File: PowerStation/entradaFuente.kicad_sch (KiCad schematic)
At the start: 0 parts

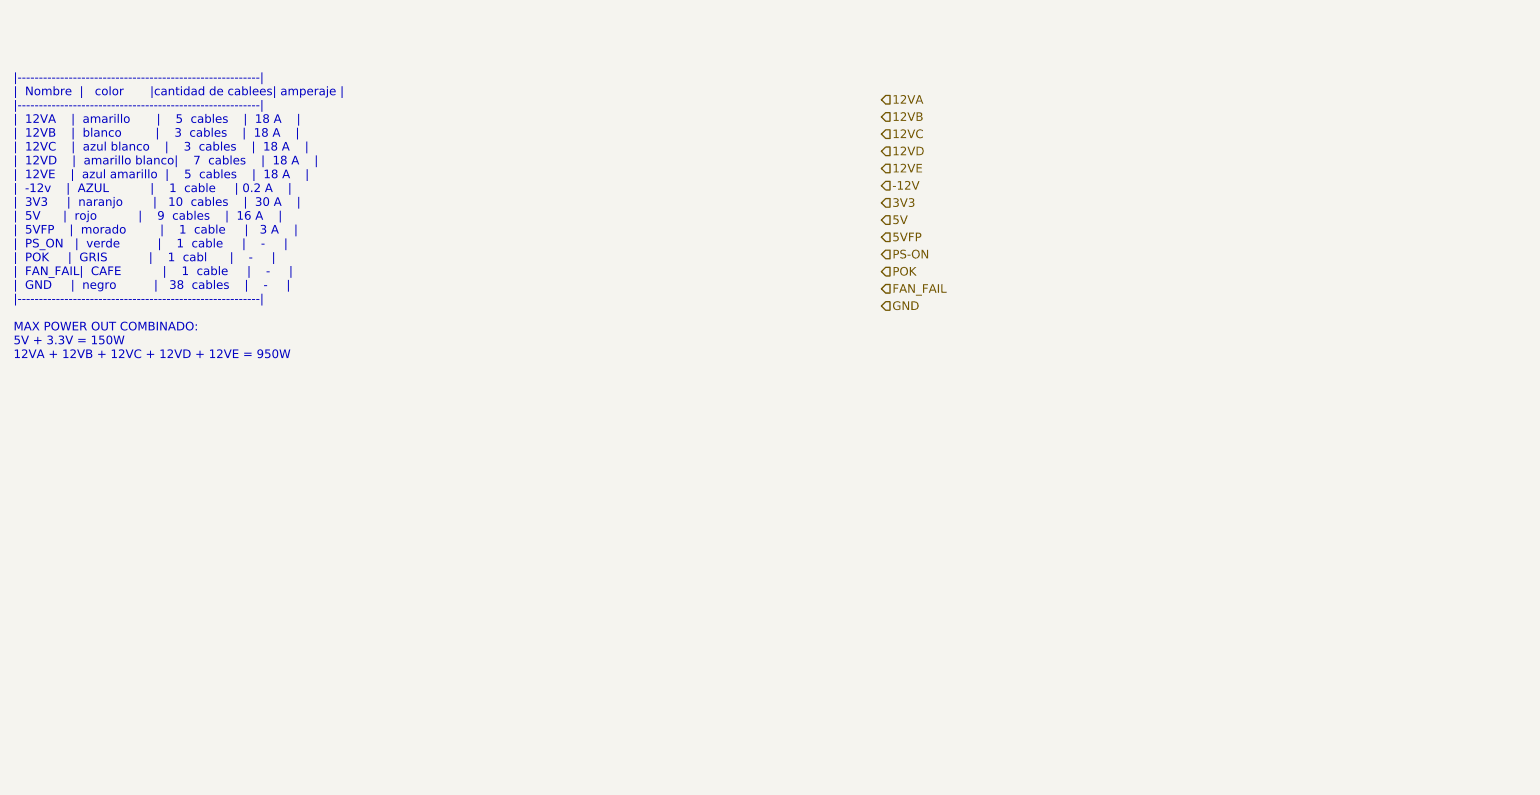
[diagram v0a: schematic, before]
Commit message: terminando diagrama
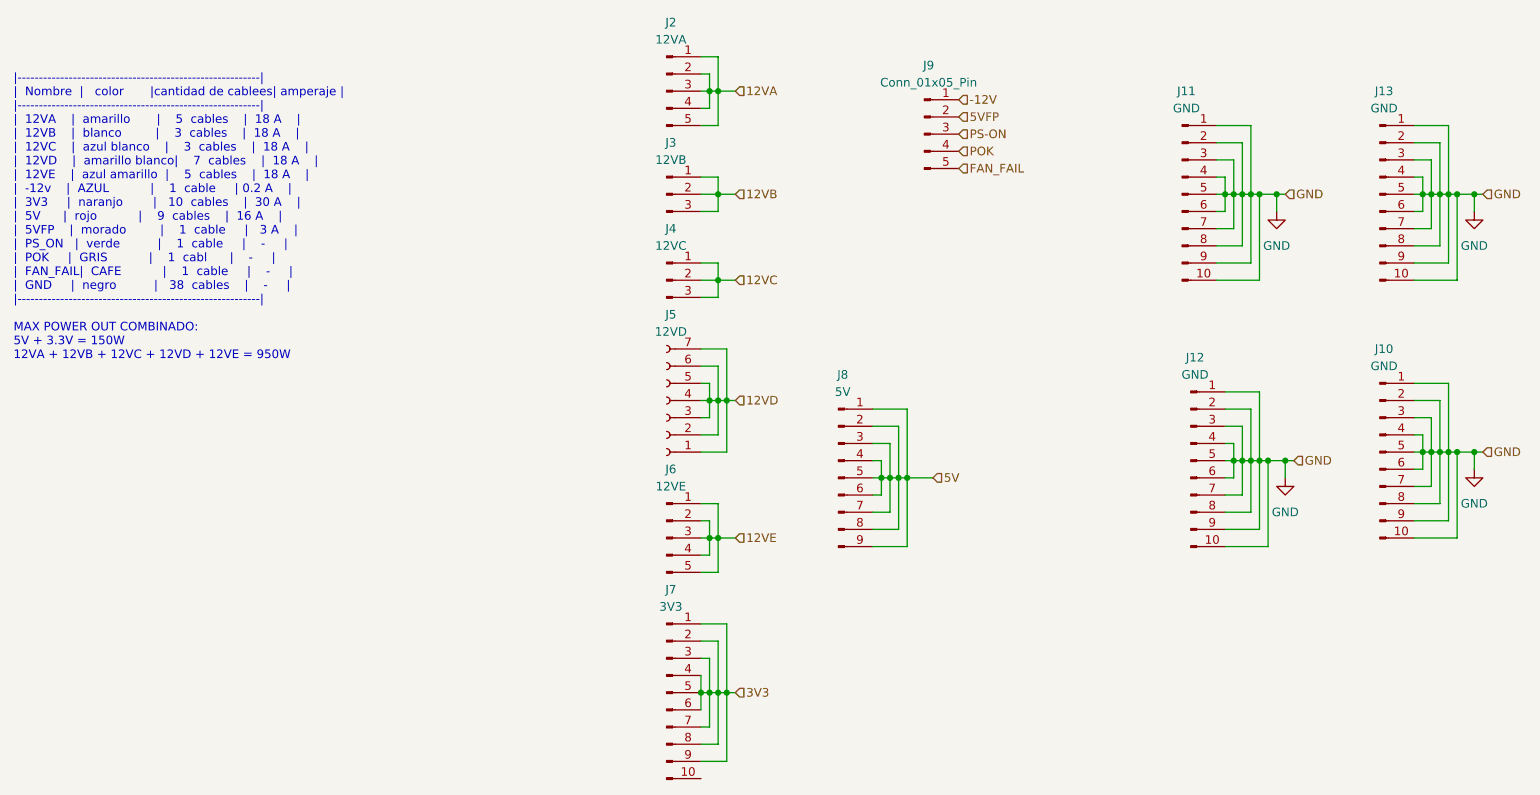
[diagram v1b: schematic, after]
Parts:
- added J10, J11, J12, J13: GND, symbol Connector:Conn_01x10_Pin
- added J2: 12VA, Connector_JST:JST_ZE_B05B-ZESK-D_1x05_P1.50mm_Vertical, symbol Connector:Conn_01x05_Pin
- added J3: 12VB, Connector_JST:JST_ZE_B03B-ZESK-D_1x03_P1.50mm_Vertical, symbol Connector:Conn_01x03_Pin
- added J4: 12VC, Connector_JST:JST_ZE_B03B-ZESK-D_1x03_P1.50mm_Vertical, symbol Connector:Conn_01x03_Pin
- added J5: 12VD, Connector_JST:JST_ZE_B07B-ZESK-D_1x07_P1.50mm_Vertical, symbol Connector:Conn_01x07_Socket
- added J6: 12VE, Connector_JST:JST_ZE_B05B-ZESK-D_1x05_P1.50mm_Vertical, symbol Connector:Conn_01x05_Pin
- added J7: 3V3, Connector_JST:JST_ZE_B10B-ZESK-D_1x10_P1.50mm_Vertical, symbol Connector:Conn_01x10_Pin
- added J8: 5V, Connector_JST:JST_ZE_B09B-ZESK-1D_1x09_P1.50mm_Vertical, symbol Connector:Conn_01x09_Pin
- added J9: Conn_01x05_Pin, Connector_JST:JST_ZE_B05B-ZESK-D_1x05_P1.50mm_Vertical, symbol Connector:Conn_01x05_Pin
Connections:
- net -12V: now also J9.1 (Pin_1)
- net 12VA: now also J2.1 (Pin_1), J2.2 (Pin_2), J2.3 (Pin_3), J2.4 (Pin_4), J2.5 (Pin_5)
- net 12VB: now also J3.1 (Pin_1), J3.2 (Pin_2), J3.3 (Pin_3)
- net 12VC: now also J4.1 (Pin_1), J4.2 (Pin_2), J4.3 (Pin_3)
- net 12VD: now also J5.1 (Pin_1), J5.2 (Pin_2), J5.3 (Pin_3), J5.4 (Pin_4), J5.5 (Pin_5), J5.6 (Pin_6), J5.7 (Pin_7)
- net 12VE: now also J6.1 (Pin_1), J6.2 (Pin_2), J6.3 (Pin_3), J6.4 (Pin_4), J6.5 (Pin_5)
- net 3V3: now also J7.1 (Pin_1), J7.2 (Pin_2), J7.3 (Pin_3), J7.4 (Pin_4), J7.5 (Pin_5), J7.6 (Pin_6), J7.7 (Pin_7), J7.8 (Pin_8), J7.9 (Pin_9)
- net 5V: now also J8.1 (Pin_1), J8.2 (Pin_2), J8.3 (Pin_3), J8.4 (Pin_4), J8.5 (Pin_5), J8.6 (Pin_6), J8.7 (Pin_7), J8.8 (Pin_8), J8.9 (Pin_9)
- net 5VFP: now also J9.2 (Pin_2)
- net FAN_FAIL: now also J9.5 (Pin_5)
- net GND: now also J10.1 (Pin_1), J10.10 (Pin_10), J10.2 (Pin_2), J10.3 (Pin_3), J10.4 (Pin_4), J10.5 (Pin_5), J10.6 (Pin_6), J10.7 (Pin_7), J10.8 (Pin_8), J10.9 (Pin_9), J11.1 (Pin_1), J11.10 (Pin_10), J11.2 (Pin_2), J11.3 (Pin_3), J11.4 (Pin_4), J11.5 (Pin_5), J11.6 (Pin_6), J11.7 (Pin_7), J11.8 (Pin_8), J11.9 (Pin_9), J12.1 (Pin_1), J12.10 (Pin_10), J12.2 (Pin_2), J12.3 (Pin_3), J12.4 (Pin_4), J12.5 (Pin_5), J12.6 (Pin_6), J12.7 (Pin_7), J12.8 (Pin_8), J12.9 (Pin_9), J13.1 (Pin_1), J13.10 (Pin_10), J13.2 (Pin_2), J13.3 (Pin_3), J13.4 (Pin_4), J13.5 (Pin_5), J13.6 (Pin_6), J13.7 (Pin_7), J13.8 (Pin_8), J13.9 (Pin_9)
- net POK: now also J9.4 (Pin_4)
- net PS-ON: now also J9.3 (Pin_3)

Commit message: avanxe en placa
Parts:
- J10, J11, J12, J13: footprint (none) -> Connector_JST:JST_ZE_B10B-ZESK-D_1x10_P1.50mm_Vertical
- J9: value Conn_01x05_Pin -> control
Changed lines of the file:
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@@
       (effects (font (size 1.27 1.27)))
     )
-    (property "Value" "Conn_01x05_Pin" (at 159.385 33.02 0)
+    (property "Value" "control" (at 159.385 33.02 0)
       (effects (font (size 1.27 1.27)))
     )
@@
       (effects (font (size 1.27 1.27)))
     )
-    (property "Footprint" "" (at 226.06 87.63 0)
+    (property "Footprint" "Connector_JST:JST_ZE_B10B-ZESK-D_1x10_P1.50mm_Vertical" (at 226.06 87.63 0)
       (effects (font (size 1.27 1.27)) hide)
     )
@@
       (effects (font (size 1.27 1.27)))
     )
-    (property "Footprint" "" (at 198.12 88.9 0)
+    (property "Footprint" "Connector_JST:JST_ZE_B10B-ZESK-D_1x10_P1.50mm_Vertical" (at 198.12 88.9 0)
       (effects (font (size 1.27 1.27)) hide)
     )
@@
       (effects (font (size 1.27 1.27)))
     )
-    (property "Footprint" "" (at 226.06 49.53 0)
+    (property "Footprint" "Connector_JST:JST_ZE_B10B-ZESK-D_1x10_P1.50mm_Vertical" (at 226.06 49.53 0)
       (effects (font (size 1.27 1.27)) hide)
     )
@@
       (effects (font (size 1.27 1.27)))
     )
-    (property "Footprint" "" (at 196.85 49.53 0)
-      (effects (font (size 1.27 1.27)) hide)
-    )
+    (property "Footprint" "Connector_JST:JST_ZE_B10B-ZESK-D_1x10_P1.50mm_Vertical" (at 196.85 49.53 0)
+      (effects (font (size 1.27 1.27)) hide)
+    )

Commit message: correccion de esquermatico y avanze en placa
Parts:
- renumbered J2 to J1, J8 to J10, J6 to J11, J7 to J12, J9 to J2, J11 to J4, J13 to J5, J4 to J6, J5 to J7, J10 to J8, J12 to J9
